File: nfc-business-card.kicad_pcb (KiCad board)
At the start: 2 copper layers, 89 x 51 mm, 9 parts, among them U1 NT3H2111W0FHKH

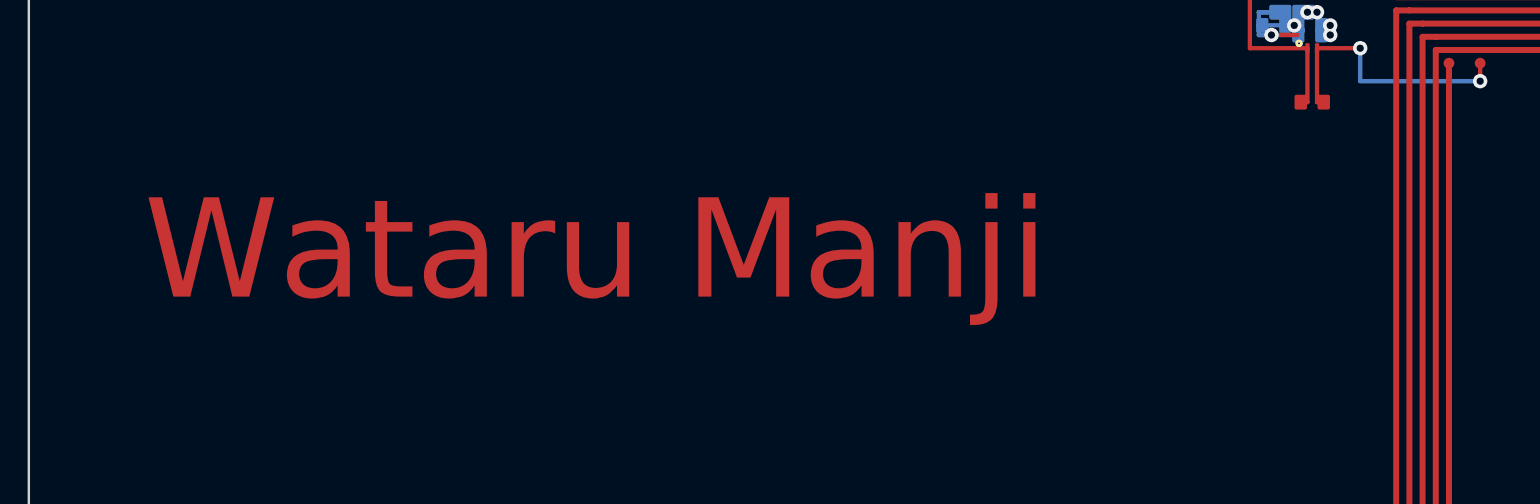
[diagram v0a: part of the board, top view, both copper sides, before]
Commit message: feat(design): Baskerville/Helvetica typography, larger type scale, centered QR block
- Font registry scripts/fonts.py: single source of truth (face -> TTF/TTC
  with index) shared by preview, KiCad bake, and layout checks
- ENIG name: Georgia Bold -> Baskerville SemiBold (cap 5.2 -> 5.5 mm)
- Silk: Arial -> Helvetica Neue (roles 1.6 -> 1.8 mm, contacts 1.5 -> 1.7 mm)
- QR + contacts block moved down (center 28.5 -> 33.0 mm): roles->QR gap
  0.05 -> 4.55 mm, left column now centered vs antenna zone
- Regenerated assets, PCB, and preview; all layout checks pass
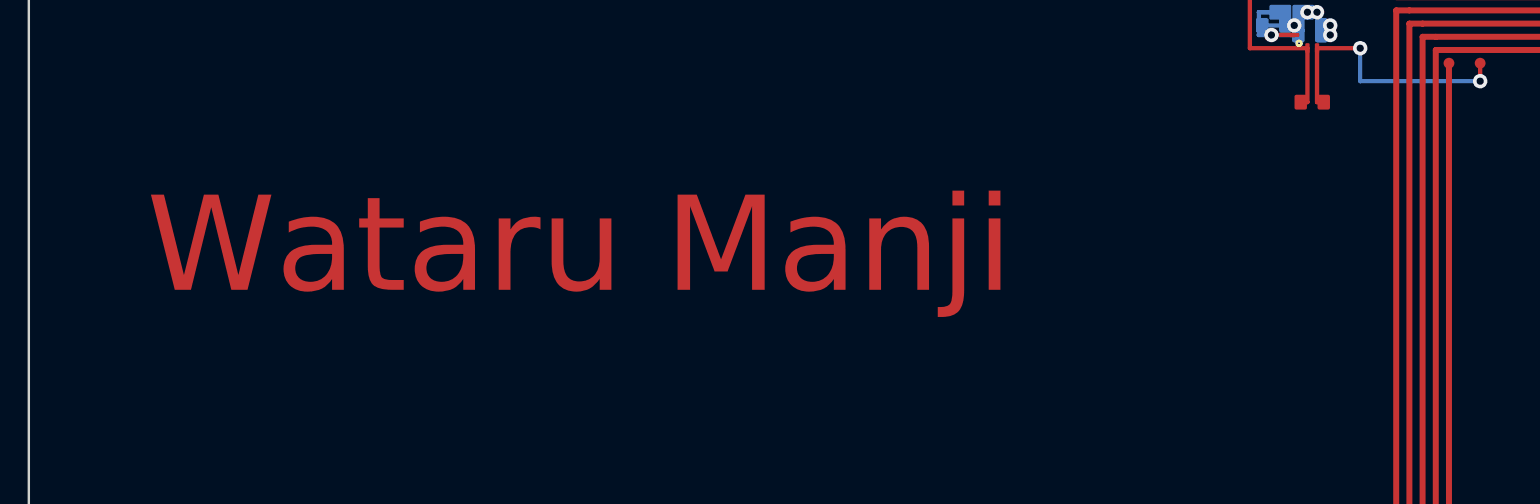
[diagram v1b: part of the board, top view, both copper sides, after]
